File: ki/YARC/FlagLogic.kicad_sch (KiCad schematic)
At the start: 13 parts, among them U105 74LS86, U106 74LS139, U107 74HC00, U108 74HC02, U109 74LS32, U110 74LS21, U111 74LS153, U112 74LS573, U113 74LS573, U114 74LS574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

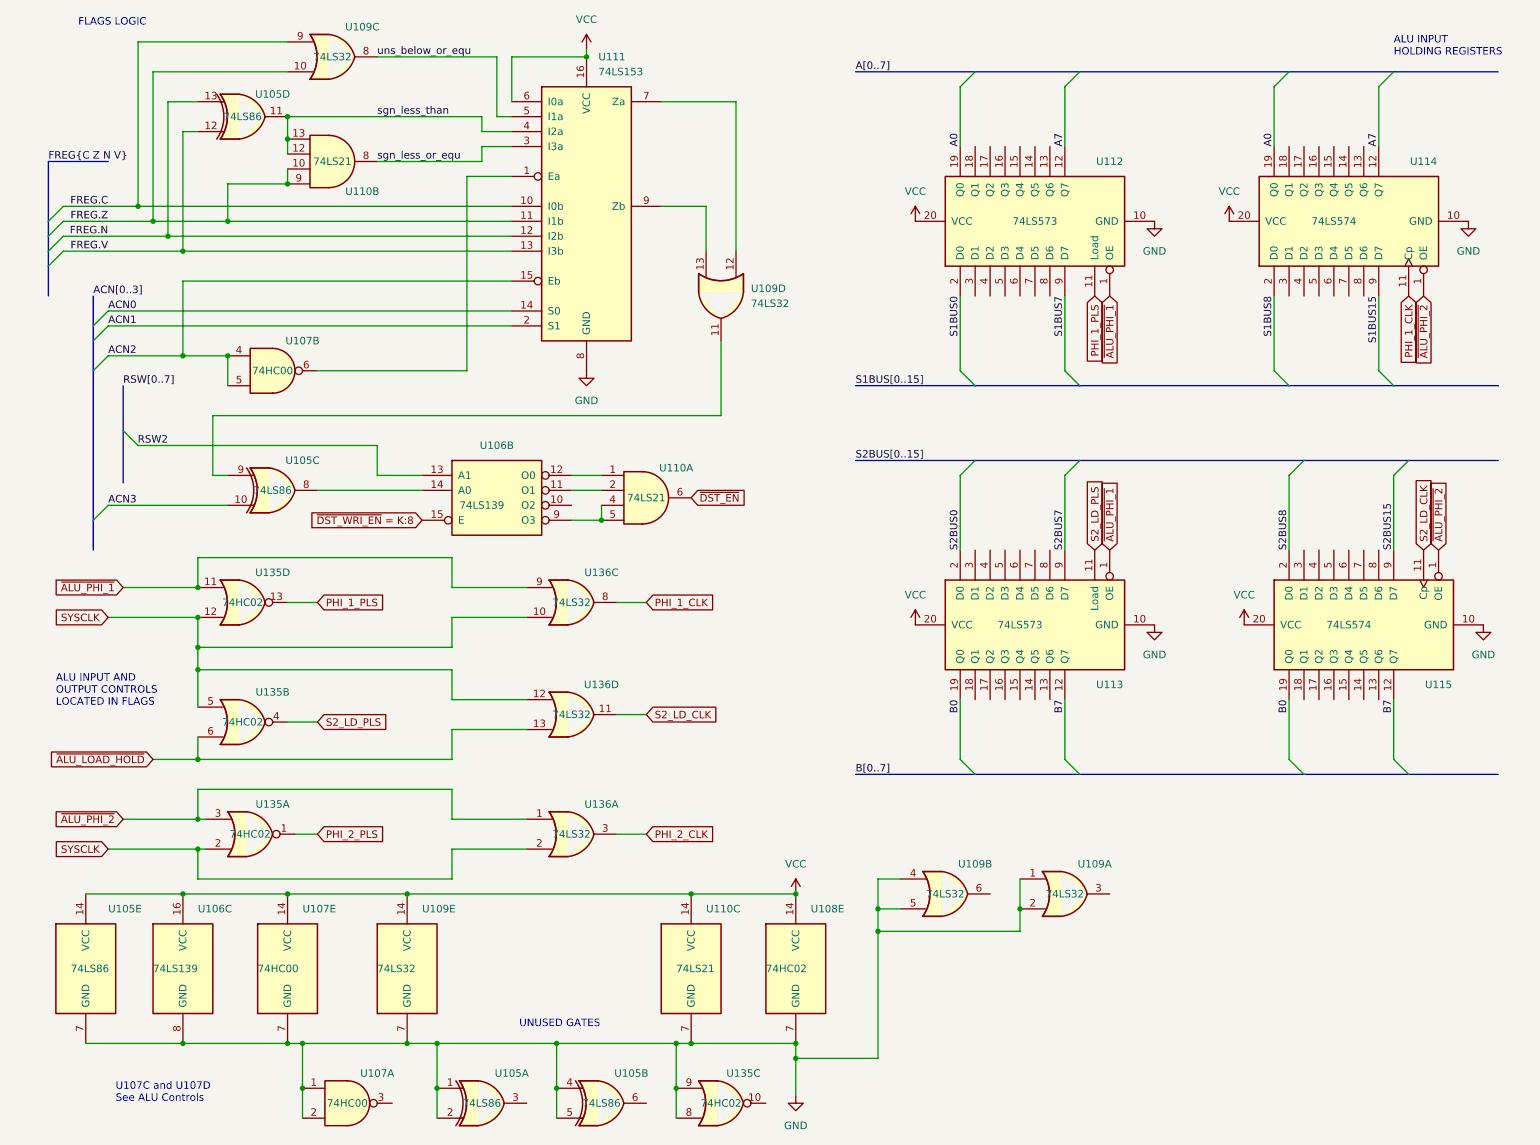
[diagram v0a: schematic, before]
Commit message: Ongoing fixes for ERC errors
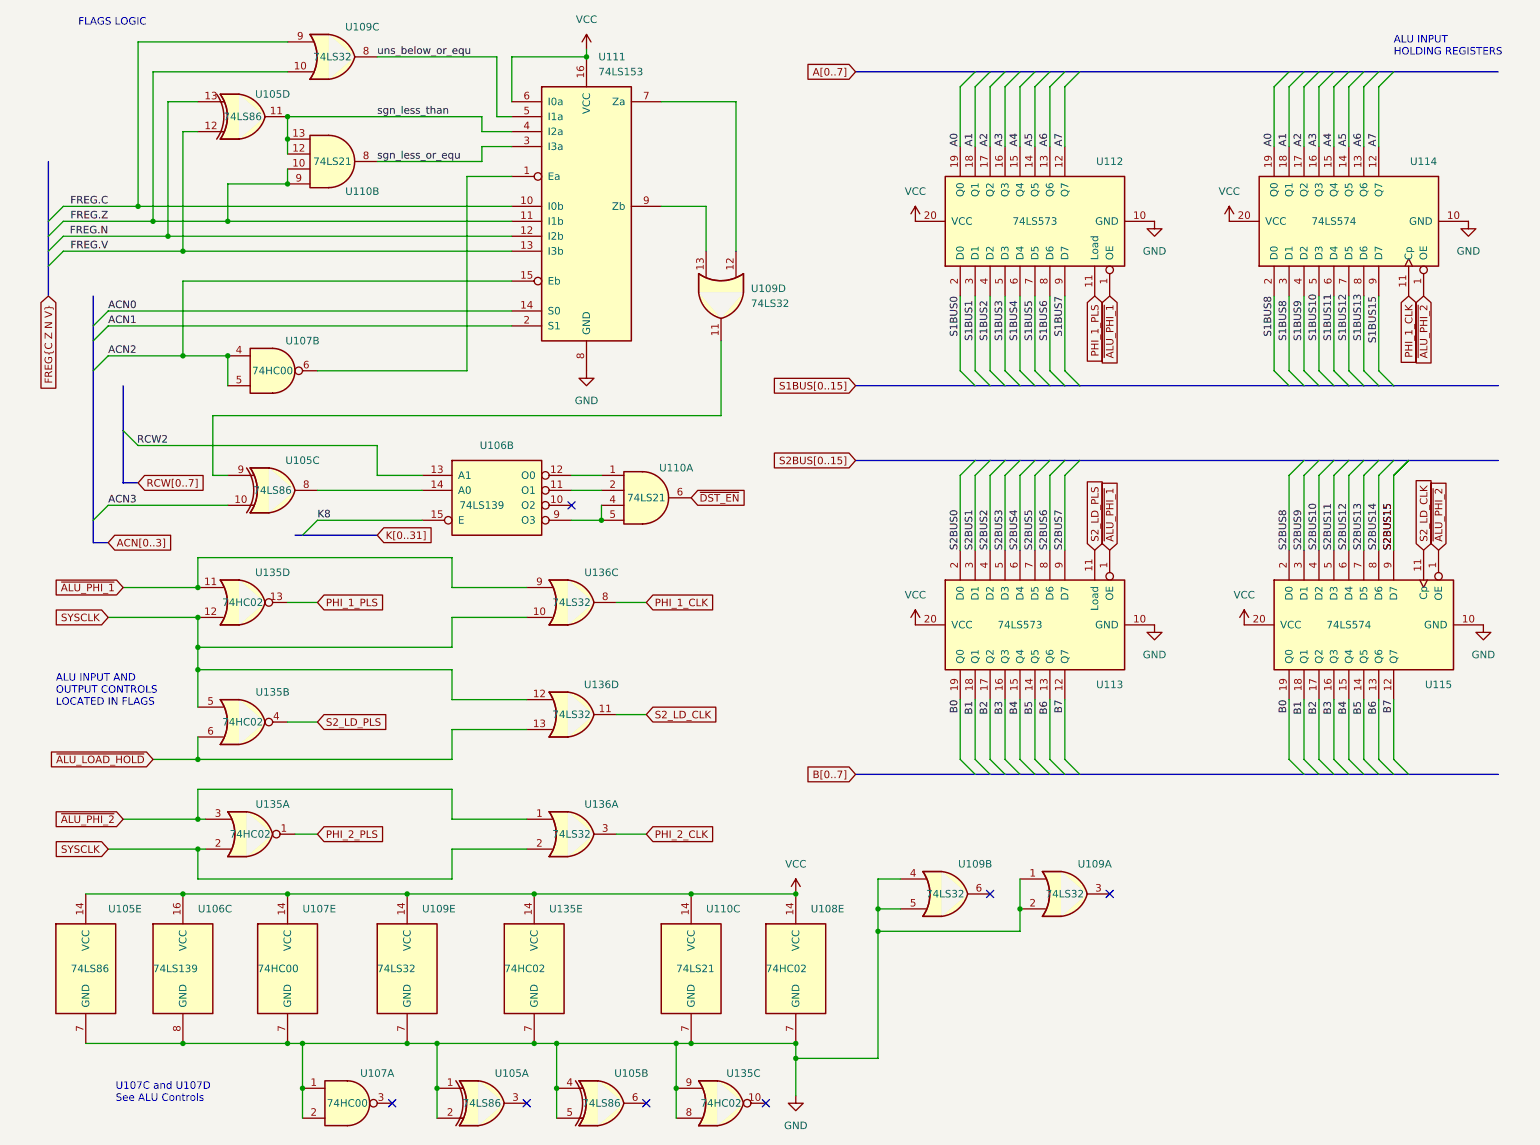
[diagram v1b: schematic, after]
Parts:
- added unit 5 of U135
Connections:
- net GND: now also U135.7 (GND)
- net S1BUS8: now also U114.3 (D1)
- net VCC: now also U135.14 (VCC)
- net A6: now reaches U112.13 (Q6)
- net A6: now also U114.13 (Q6)
- net A5: now reaches U112.14 (Q5)
- net A5: now also U114.14 (Q5)
- net A4: now reaches U112.15 (Q4)
- net A4: now also U114.15 (Q4)
- net A3: now reaches U112.16 (Q3)
- net A3: now also U114.16 (Q3)
- net A2: now reaches U112.17 (Q2)
- net A2: now also U114.17 (Q2)
- net A1: now reaches U112.18 (Q1)
- net A1: now also U114.18 (Q1)
- net S1BUS1: now reaches U112.3 (D1)
- net S1BUS2: now reaches U112.4 (D2)
- net S1BUS3: now reaches U112.5 (D3)
- net S1BUS4: now reaches U112.6 (D4)
- net S1BUS5: now reaches U112.7 (D5)
- net S1BUS6: now reaches U112.8 (D6)
- net S1BUS9: now reaches U114.4 (D2)
- net S1BUS10: now reaches U114.5 (D3)
- net S1BUS11: now reaches U114.6 (D4)
- net S1BUS12: now reaches U114.7 (D5)
- net S1BUS13: now reaches U114.8 (D6)
- net B6: now reaches U113.13 (Q6)
- net B6: now also U115.13 (Q6)
- net B5: now reaches U113.14 (Q5)
- net B5: now also U115.14 (Q5)
- net B4: now reaches U113.15 (Q4)
- net B4: now also U115.15 (Q4)
- net B3: now reaches U113.16 (Q3)
- net B3: now also U115.16 (Q3)
- net B2: now reaches U113.17 (Q2)
- net B2: now also U115.17 (Q2)
- net B1: now reaches U113.18 (Q1)
- net B1: now also U115.18 (Q1)
- net S2BUS1: now reaches U113.3 (D1)
- net S2BUS2: now reaches U113.4 (D2)
- net S2BUS3: now reaches U113.5 (D3)
- net S2BUS4: now reaches U113.6 (D4)
- net S2BUS5: now reaches U113.7 (D5)
- net S2BUS6: now reaches U113.8 (D6)
- net S2BUS9: now reaches U115.3 (D1)
- net S2BUS10: now reaches U115.4 (D2)
- net S2BUS11: now reaches U115.5 (D3)
- net S2BUS12: now reaches U115.6 (D4)
- net S2BUS13: now reaches U115.7 (D5)
- net S2BUS14: now reaches U115.8 (D6)
- net RSW2 renamed RCW2
- net ~{DST_WRI_EN} = K:8 renamed K8
- no-connect marks 0 -> 7
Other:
- note removed: "UNUSED GATES"

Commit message: Ongoing schematic changes
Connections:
- net RCW2 renamed DST:2
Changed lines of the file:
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@@
-    (stroke (width 0) (type default))
-  )
-  (bus_entry (at 27.94 83.82) (size 2.54 2.54)
     (stroke (width 0) (type default))
   )
@@
     (stroke (width 0) (type default))
   )
-  (bus (pts (xy 25.4 102.87) (xy 22.86 102.87))
+  (bus (pts (xy 25.4 101.6) (xy 22.86 101.6))
     (stroke (width 0) (type default))
   )
@@
     (stroke (width 0) (type default))
   )
-  (bus (pts (xy 152.4 88.9) (xy 172.72 88.9))
+  (bus (pts (xy 165.1 88.9) (xy 172.72 88.9))
     (stroke (width 0) (type default))
   )
@@
     (stroke (width 0) (type default))
   )
-  (bus (pts (xy 152.4 76.2) (xy 172.72 76.2))
+  (bus (pts (xy 165.1 76.2) (xy 172.72 76.2))
     (stroke (width 0) (type default))
   )
@@
     (stroke (width 0) (type default))
   )
-  (bus (pts (xy 152.4 142.24) (xy 172.72 142.24))
+  (bus (pts (xy 165.1 142.24) (xy 172.72 142.24))
     (stroke (width 0) (type default))
   )
@@
     (stroke (width 0) (type default))
   )
-  (bus (pts (xy 27.94 76.2) (xy 27.94 83.82))
-    (stroke (width 0) (type default))
-  )
   (wire (pts (xy 55.88 36.83) (xy 55.88 34.29))
     (stroke (width 0) (type default))
@@
     (stroke (width 0) (type default))
   )
-  (bus (pts (xy 58.42 101.6) (xy 71.12 101.6))
+  (bus (pts (xy 58.42 101.6) (xy 67.31 101.6))
     (stroke (width 0) (type default))
   )
@@
     (stroke (width 0) (type default))
   )
-  (bus (pts (xy 27.94 83.82) (xy 27.94 92.71))
-    (stroke (width 0) (type default))
-  )
-  (bus (pts (xy 22.86 102.87) (xy 22.86 99.06))
+  (bus (pts (xy 22.86 101.6) (xy 22.86 99.06))
     (stroke (width 0) (type default))
   )
@@
     (stroke (width 0) (type default))
   )
-  (wire (pts (xy 71.12 91.44) (xy 71.12 86.36))
-    (stroke (width 0) (type default))
-  )
   (wire (pts (xy 40.64 120.65) (xy 40.64 124.46))
     (stroke (width 0) (type default))
@@
     (stroke (width 0) (type default))
   )
-  (bus (pts (xy 152.4 22.86) (xy 172.72 22.86))
+  (bus (pts (xy 165.1 22.86) (xy 172.72 22.86))
     (stroke (width 0) (type default))
   )
@@
     (stroke (width 0) (type default))
   )
-  (wire (pts (xy 30.48 86.36) (xy 71.12 86.36))
-    (stroke (width 0) (type default))
-  )
   (wire (pts (xy 156.21 160.02) (xy 156.21 165.1))
     (stroke (width 0) (type default))
@@
   )
   (wire (pts (xy 238.76 91.44) (xy 238.76 104.14))
-    (stroke (width 0) (type default))
-  )
-  (bus (pts (xy 27.94 92.71) (xy 30.48 92.71))
     (stroke (width 0) (type default))
   )
@@
     (effects (font (size 1.27 1.27)) (justify left bottom))
   )
-  (label "RCW2" (at 35.56 86.36 180) (fields_autoplaced)
-    (effects (font (size 1.27 1.27)) (justify right bottom))
-  )
   (label "S2BUS15" (at 243.84 104.14 90) (fields_autoplaced)
     (effects (font (size 1.27 1.27)) (justify left bottom))
@@
     (effects (font (size 1.27 1.27)) (justify left bottom))
   )
-  (global_label "B[0..7]" (shape input) (at 152.4 142.24 180) (fields_autoplaced)
+  (global_label "B[0..7]" (shape input) (at 165.1 142.24 180) (fields_autoplaced)
     (effects (font (size 1.27 1.27)) (justify right))
-    (property "Intersheetrefs" "${INTERSHEET_REFS}" (at 142.8228 142.24 0)
+    (property "Intersheetrefs" "${INTERSHEET_REFS}" (at 155.5228 142.24 0)
       (effects (font (size 1.27 1.27)) (justify right) hide)
     )
@@
     )
   )
-  (global_label "K[0..31]" (shape input) (at 71.12 101.6 0) (fields_autoplaced)
+  (global_label "K[0..31]" (shape input) (at 67.31 101.6 0) (fields_autoplaced)
     (effects (font (size 1.27 1.27)) (justify left))
-    (property "Intersheetrefs" "${INTERSHEET_REFS}" (at 81.9067 101.6 0)
+    (property "Intersheetrefs" "${INTERSHEET_REFS}" (at 78.0967 101.6 0)
       (effects (font (size 1.27 1.27)) (justify left) hide)
     )
@@
     )
   )
-  (global_label "S1BUS[0..15]" (shape input) (at 152.4 76.2 180) (fields_autoplaced)
+  (global_label "S1BUS[0..15]" (shape input) (at 165.1 76.2 180) (fields_autoplaced)
     (effects (font (size 1.27 1.27)) (justify right))
-    (property "Intersheetrefs" "${INTERSHEET_REFS}" (at 136.6543 76.2 0)
+    (property "Intersheetrefs" "${INTERSHEET_REFS}" (at 149.3543 76.2 0)
       (effects (font (size 1.27 1.27)) (justify right) hide)
     )
@@
     )
   )
-  (global_label "RCW[0..7]" (shape input) (at 30.48 92.71 0) (fields_autoplaced)
-    (effects (font (size 1.27 1.27)) (justify left))
-    (property "Intersheetrefs" "${INTERSHEET_REFS}" (at 42.7786 92.71 0)
-      (effects (font (size 1.27 1.27)) (justify left) hide)
-    )
-  )
-  (global_label "S2BUS[0..15]" (shape input) (at 152.4 88.9 180) (fields_autoplaced)
+  (global_label "S2BUS[0..15]" (shape input) (at 165.1 88.9 180) (fields_autoplaced)
     (effects (font (size 1.27 1.27)) (justify right))
-    (property "Intersheetrefs" "${INTERSHEET_REFS}" (at 136.6543 88.9 0)
+    (property "Intersheetrefs" "${INTERSHEET_REFS}" (at 149.3543 88.9 0)
       (effects (font (size 1.27 1.27)) (justify right) hide)
     )
@@
     )
   )
+  (global_label "DST:2" (shape input) (at 71.12 91.44 180) (fields_autoplaced)
+    (effects (font (size 1.27 1.27)) (justify right))
+    (property "Intersheetrefs" "${INTERSHEET_REFS}" (at 62.8734 91.44 0)
+      (effects (font (size 1.27 1.27)) (justify right) hide)
+    )
+  )
   (global_label "~{DST_EN}" (shape input) (at 124.46 95.25 0) (fields_autoplaced)
     (effects (font (size 1.27 1.27)) (justify left))
@@
     )
   )
-  (global_label "ACN[0..3]" (shape input) (at 25.4 102.87 0) (fields_autoplaced)
+  (global_label "ACN[0..3]" (shape input) (at 25.4 101.6 0) (fields_autoplaced)
     (effects (font (size 1.27 1.27)) (justify left))
-    (property "Intersheetrefs" "${INTERSHEET_REFS}" (at 37.3963 102.87 0)
+    (property "Intersheetrefs" "${INTERSHEET_REFS}" (at 37.3963 101.6 0)
       (effects (font (size 1.27 1.27)) (justify left) hide)
     )
   )
-  (global_label "A[0..7]" (shape input) (at 152.4 22.86 180) (fields_autoplaced)
+  (global_label "A[0..7]" (shape input) (at 165.1 22.86 180) (fields_autoplaced)
     (effects (font (size 1.27 1.27)) (justify right))
-    (property "Intersheetrefs" "${INTERSHEET_REFS}" (at 143.0042 22.86 0)
+    (property "Intersheetrefs" "${INTERSHEET_REFS}" (at 155.7042 22.86 0)
       (effects (font (size 1.27 1.27)) (justify right) hide)
     )

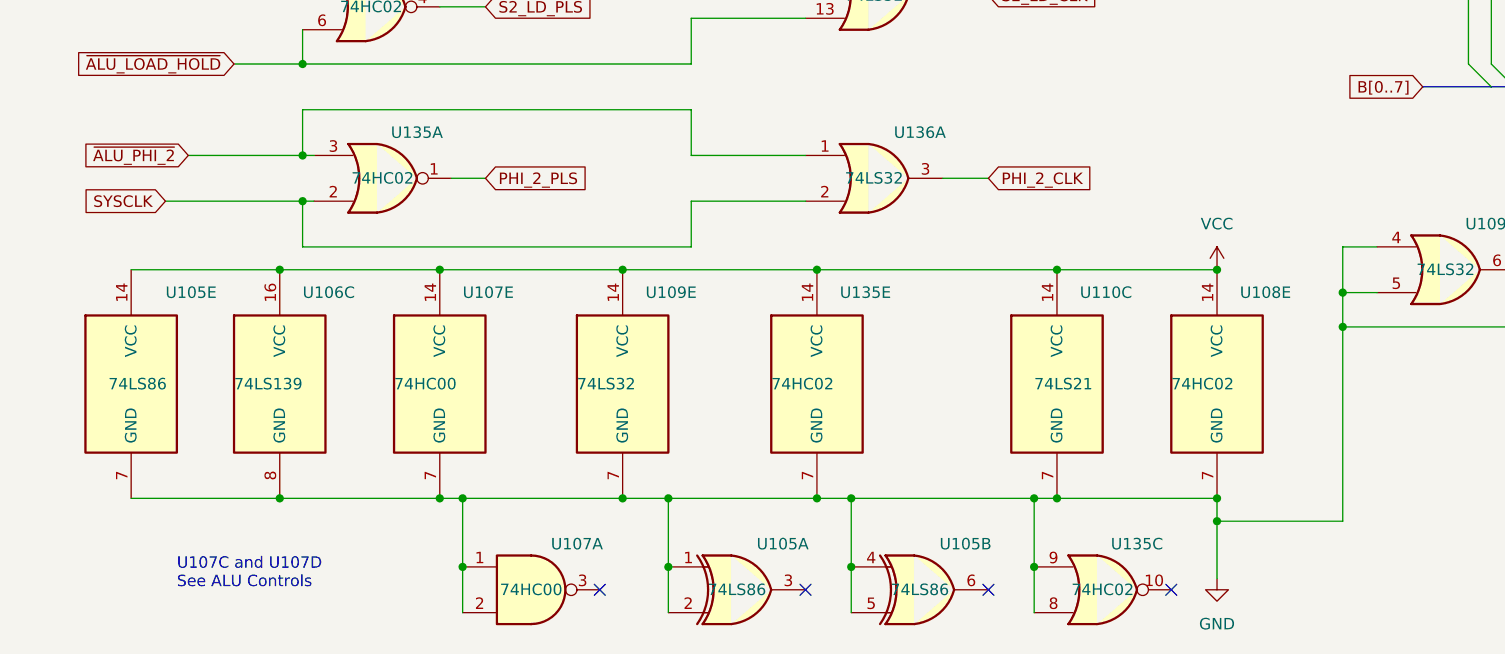
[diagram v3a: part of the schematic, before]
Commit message: Schematic for addressing unit is complete and all ERC violations addressed
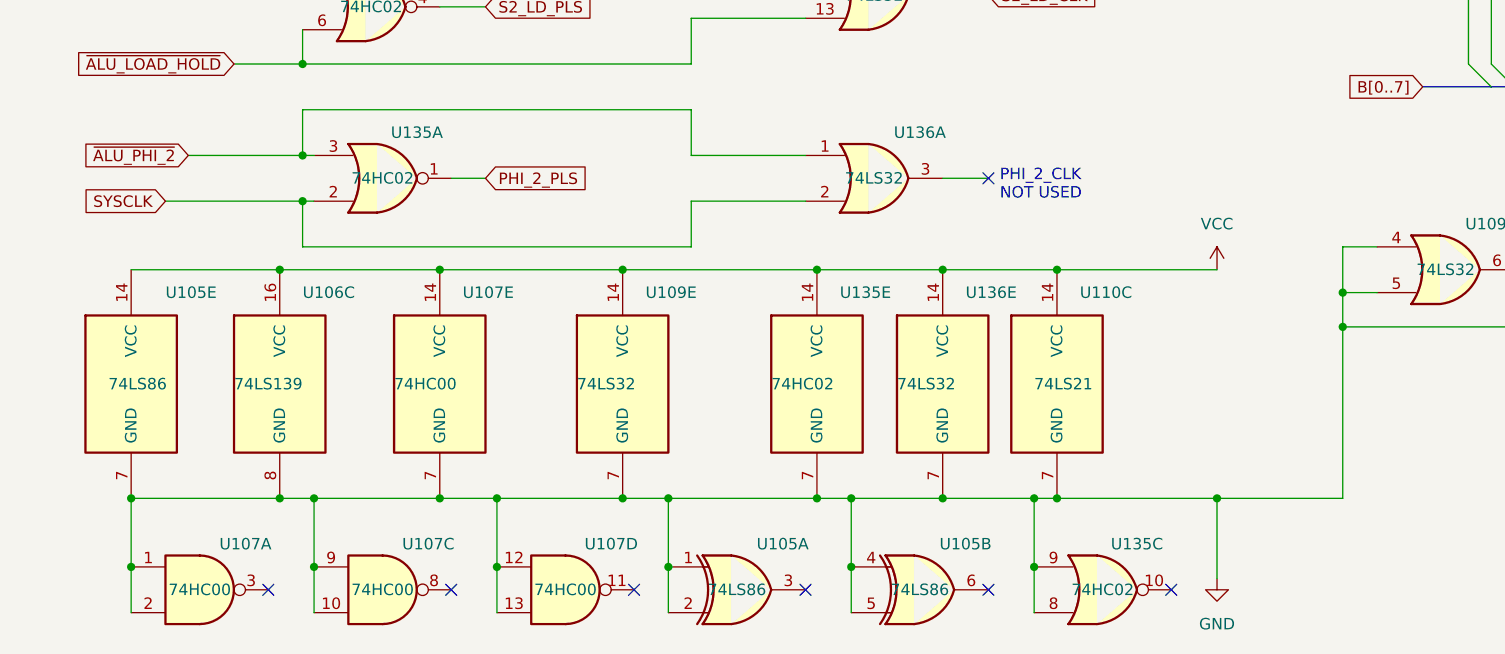
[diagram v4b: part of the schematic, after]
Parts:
- removed U108: 74HC02, symbol 74xx:74HC02
- added unit 4 of U107
- added unit 3 of U107
- added unit 5 of U136
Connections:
- net GND: now also U107.10, U107.12, U107.13, U107.9, U136.7 (GND)
- net VCC: now also U136.14 (VCC)
- net PHI_2_CLK: no longer names the net of U136.3
- no-connect marks 7 -> 10
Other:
- note added: "PHI_2_CLK NOT USED"
- note removed: "U107C and U107D See ALU Controls"
- moved on the sheet: U107A
